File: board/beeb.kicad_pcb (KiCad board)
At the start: 2 copper layers, 76.2 x 53.3 mm, 54 parts, among them J2 AVR-JTAG-10, SW1 SW_DIP_x08, U1 WIT122UH, U2 ps2, U3 XC95144XL-TQ100, U4 beebKB, U5 LM1117-3.3, U6 74LS244_Split, U7 74LS244_Split, U8 LM2903

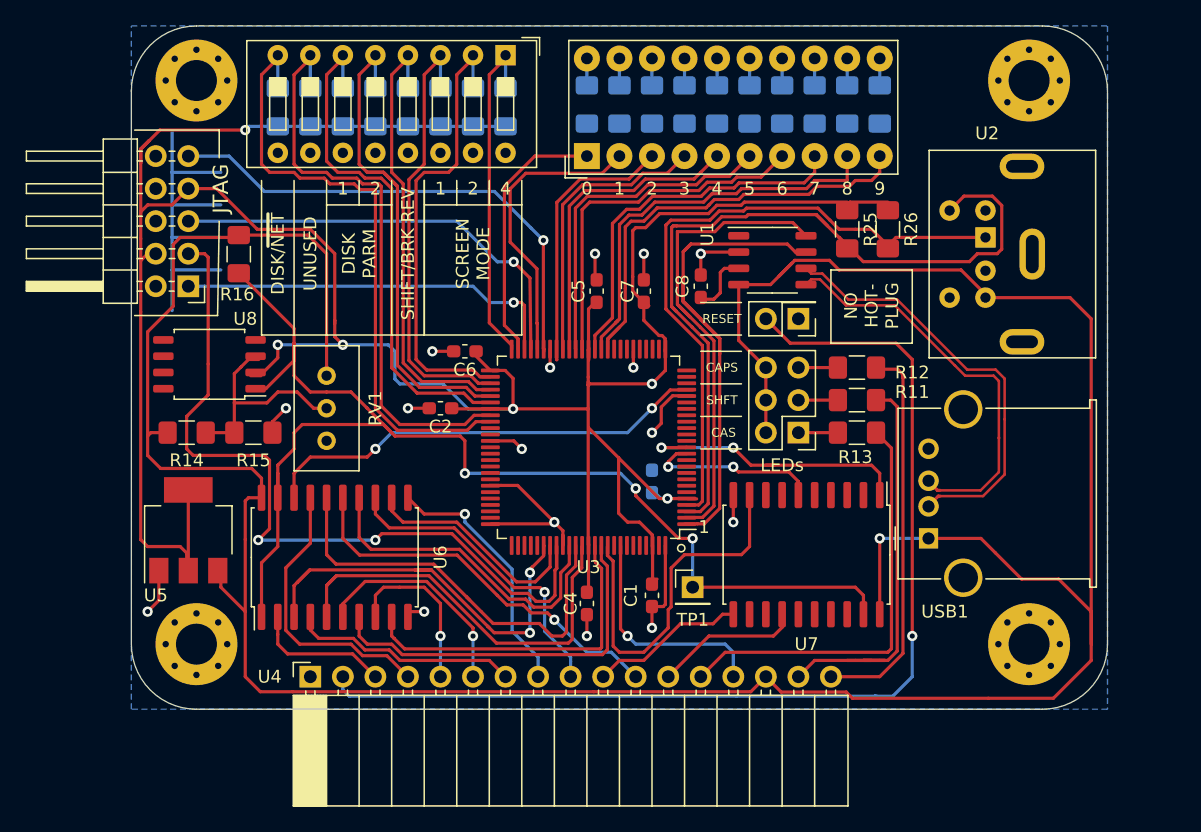
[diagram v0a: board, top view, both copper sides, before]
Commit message: Remove USB connector, move JTAG connector, mess about
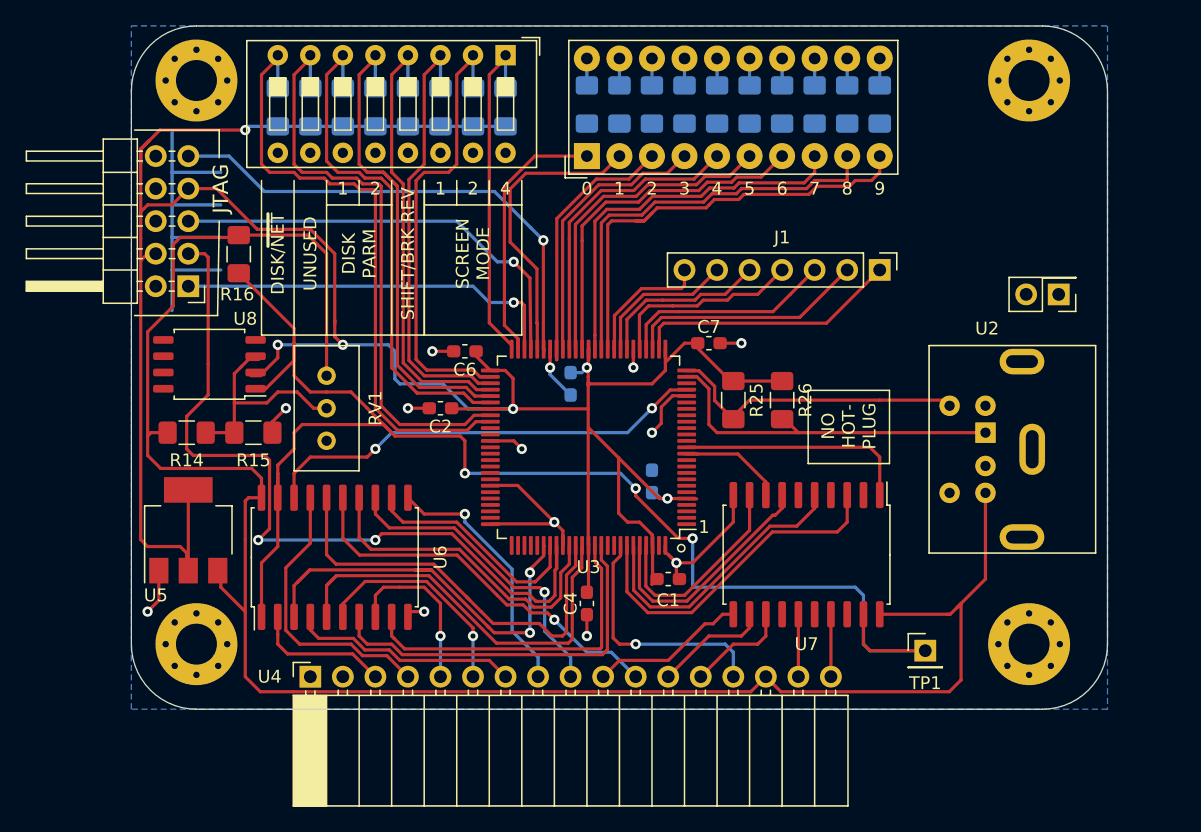
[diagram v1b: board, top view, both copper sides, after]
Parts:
- removed C8: 0.1uF, Capacitor_SMD:C_0603_1608Metric_Pad1.05x0.95mm_HandSolder
- removed LEDS1: J1, Connector_PinHeader_2.54mm:PinHeader_2x03_P2.54mm_Vertical
- removed R11, R12, R13: 470, Resistor_SMD:R_1206_3216Metric_Pad1.42x1.75mm_HandSolder
- removed U1: WIT122UH, Package_SO:SOP-8_3.9x4.9mm_P1.27mm
- removed USB1: USB, Connector_USB:USB_A_Molex_67643_Horizontal
- added J1: EXT, Connector_PinHeader_2.54mm:PinHeader_1x07_P2.54mm_Vertical, F.Cu at (105.4, 97.8)
- C5: moved to B.Cu
- moved RESET1 20.4 mm to (119.4, 99.7)
- moved TP1 18.8 mm to (109.0, 127.5)
- moved R25 16.0 mm to (94.0, 108.0)
- moved R26 15.7 mm to (97.8, 108.0)
- moved U2 15.2 mm to (113.7, 110.5)
- moved C5 7.52 mm to (81.3, 106.7), turned to 270 degrees
- moved C7 6.51 mm to (92.1, 103.5), turned to 0 degrees
- moved C1 1.80 mm to (88.9, 121.9), turned to 0 degrees
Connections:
- RESET1 pad 2: Net-(RESET1-Pad2) -> (no net)
- U3 pad 1: /PS2DATA_B -> (no net)
- U3 pad 2: /PS2CLK_B -> (no net)
- U3 pad 24: (no net) -> /PS2DATA_A
- U3 pad 25: (no net) -> /PS2CLK_A
- U3 pad 27: (no net) -> Net-(J1-Pad1)
- U3 pad 28: (no net) -> Net-(J1-Pad2)
- U3 pad 29: (no net) -> Net-(J1-Pad3)
- U3 pad 3: /PS2CLK_A -> (no net)
- U3 pad 30: (no net) -> Net-(J1-Pad4)
- U3 pad 32: (no net) -> Net-(J1-Pad5)
- U3 pad 33: (no net) -> Net-(J1-Pad6)
- U3 pad 34: (no net) -> Net-(J1-Pad7)
- U3 pad 4: /PS2DATA_A -> (no net)
- U3 pad 91: /ROW2_BUF -> (no net)
- U3 pad 94: (no net) -> /LED_CAPS_BUF
- U3 pad 95: (no net) -> /LED_SHIFT_BUF
- U3 pad 96: (no net) -> /LED_CAS_BUF
- U3 pad 97: (no net) -> /ROW2_BUF
- U4 pad 13: Net-(R13-Pad2) -> Net-(U4-Pad13)
- U4 pad 16: Net-(R11-Pad2) -> Net-(U4-Pad16)
- U4 pad 17: Net-(R12-Pad2) -> Net-(U4-Pad17)
- U4 pad 2: Net-(RESET1-Pad2) -> (no net)
- U7 pad 12: (no net) -> /W
- U7 pad 13: (no net) -> Net-(U4-Pad13)
- U7 pad 14: /W -> (no net)
- U7 pad 15: (no net) -> Net-(U4-Pad16)
- U7 pad 17: (no net) -> Net-(U4-Pad17)
- U7 pad 3: (no net) -> /LED_CAPS_BUF
- U7 pad 5: (no net) -> /LED_SHIFT_BUF
- U7 pad 6: /W_BUF -> (no net)
- U7 pad 7: (no net) -> /LED_CAS_BUF
- U7 pad 8: (no net) -> /W_BUF
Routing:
- net +5V: track 241.3 -> 153.4 mm, vias 1 -> 0
- net Net-(RESET1-Pad2): track 83.9 -> 0.00 mm, vias 1 -> 0
- net /PS2DATA_B: track 43.5 -> 0.00 mm
- net /PS2CLK_A: track 63.9 -> 24.2 mm
- net /PS2CLK_B: track 37.3 -> 0.00 mm
- net Net-(R11-Pad2): track 34.8 -> 0.00 mm
- net /USB_N: track 33.7 -> 0.00 mm
- net Net-(R13-Pad2): track 33.2 -> 0.00 mm
- net /USB_P: track 32.0 -> 0.00 mm
- net Net-(R12-Pad2): track 30.3 -> 0.00 mm
- net /LED_CAPS_BUF: track 0.00 -> 26.3 mm
- net +3V3: track 233.7 -> 210.0 mm
- net /PS2DATA_A: track 51.1 -> 28.7 mm
- net /LED_SHIFT_BUF: track 0.00 -> 22.3 mm
- net Net-(J1-Pad1): track 0.00 -> 20.9 mm
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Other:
- board text removed: "CAPS"
- board text removed: "CAS"
- board text removed: "LEDs"
- board text removed: "RESET"
- board text removed: "SHFT"

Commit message: Add reset line, remov vref pot
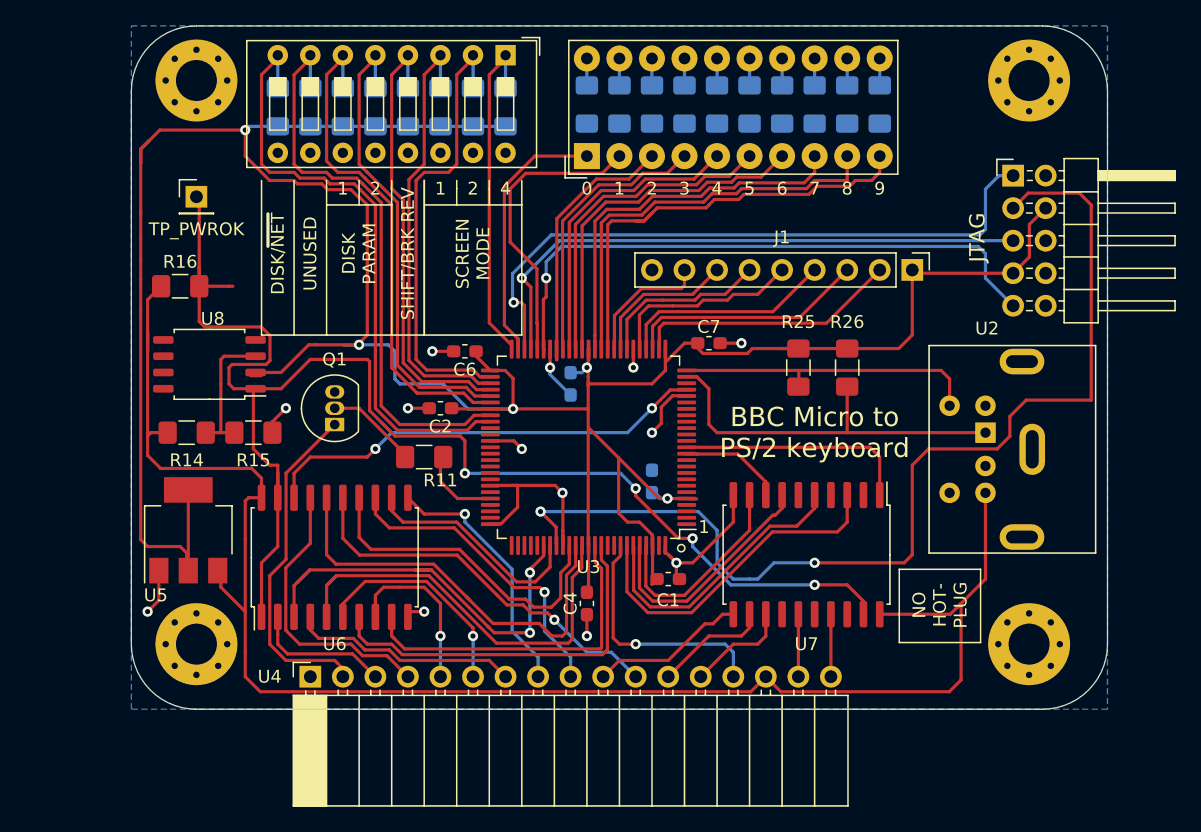
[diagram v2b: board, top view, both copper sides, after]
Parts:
- removed RESET1: J3, Connector_PinHeader_2.54mm:PinHeader_2x01_P2.54mm_Vertical
- removed RV1: R_POT, Potentiometer_THT:Potentiometer_Bourns_3386C_Horizontal
- added Q1: BC337, Package_TO_SOT_THT:TO-92_Inline, F.Cu at (62.9, 109.9)
- added R11: 220, Resistor_SMD:R_1206_3216Metric_Pad1.42x1.75mm_HandSolder, F.Cu at (69.8, 112.4)
- J1: value EXT -> Conn_01x09_Male; footprint Connector_PinHeader_2.54mm:PinHeader_1x07_P2.54mm_Vertical -> Connector_PinHeader_2.54mm:PinHeader_1x09_P2.54mm_Vertical
- moved TP1 67.0 mm to (52.1, 92.1)
- moved J2 65.0 mm to (115.8, 90.4), turned to 0 degrees
- moved R25 5.68 mm to (99.1, 105.4)
- moved R26 5.68 mm to (102.9, 105.4)
- moved R16 5.21 mm to (50.8, 99.1), turned to 0 degrees
- moved J1 2.54 mm to (108.0, 97.8)
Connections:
- J1 pad 1: Net-(J1-Pad1) -> +3V3
- U3 pad 27: Net-(J1-Pad1) -> Net-(J1-Pad2)
- U3 pad 28: Net-(J1-Pad2) -> Net-(J1-Pad3)
- U3 pad 29: Net-(J1-Pad3) -> Net-(J1-Pad4)
- U3 pad 30: Net-(J1-Pad4) -> Net-(J1-Pad5)
- U3 pad 32: Net-(J1-Pad5) -> Net-(J1-Pad6)
- U3 pad 33: Net-(J1-Pad6) -> Net-(J1-Pad7)
- U3 pad 34: Net-(J1-Pad7) -> Net-(J1-Pad8)
- U3 pad 71: (no net) -> /RST
- U4 pad 2: (no net) -> Net-(Q1-Pad1)
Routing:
- net +3V3: track 210.0 -> 238.5 mm, vias 6 -> 5
- net GND: track 84.4 -> 56.7 mm
- net Net-(Q1-Pad1): track 0.00 -> 26.4 mm
- net +5V: track 153.4 -> 128.1 mm
- net Net-(J1-Pad1): track 20.9 -> 0.00 mm
- net /TDO: track 62.2 -> 82.9 mm
- net /TCK: track 30.3 -> 50.7 mm
- net /TMS: track 34.7 -> 45.4 mm
- net Net-(J1-Pad8): track 0.00 -> 10.3 mm
- net /TDI: track 39.1 -> 47.1 mm
- net Net-(Q1-Pad2): track 0.00 -> 7.20 mm
- net Net-(R14-Pad2): track 17.4 -> 10.9 mm
- net /RST: track 0.00 -> 6.35 mm
- net Net-(R20-Pad2): track 41.6 -> 36.8 mm
- net Net-(J1-Pad2): track 18.8 -> 20.9 mm
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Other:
- board text added: "BBC Micro to PS/2 keyboard"
- board text added: "DISK PARAM"
- board text removed: "BBC Micro to PS/2 and USB keyboard"
- board text removed: "DISK PARM"

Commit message: Connect U8 to power/gnd, change U6 and U7 footprint, add TP_CLKBUF, tidy
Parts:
- added TP2: TP_CLKBUF, Connector_PinHeader_2.54mm:PinHeader_1x01_P2.54mm_Vertical, F.Cu at (95.2, 108.0)
- Q1: footprint Package_TO_SOT_THT:TO-92_Inline -> Package_TO_SOT_THT:TO-92_Inline_Wide
- U6, U7: footprint Package_SO:SOIC-20W_7.5x12.8mm_P1.27mm -> beeb:beeb_SO-20_5.3x12.6mm_P1.27mm
- U8: footprint Package_SO:SOP-8_5.28x5.23mm_P1.27mm -> Package_SO:SOP-8_3.76x4.96mm_P1.27mm
- moved Q1 1.27 mm to (62.9, 111.1)
- moved R16 0.64 mm to (50.8, 98.4)
- moved U8 0.46 mm to (53.3, 104.8), turned to 270 degrees
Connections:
- U8 pad 4: (no net) -> GND
- U8 pad 8: (no net) -> +5V
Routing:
- net /PWROK: track 112.8 -> 101.7 mm
- net +5V: track 128.1 -> 137.6 mm
- net /TCK: track 50.7 -> 57.0 mm
- net /BEEBCLK_BUF: track 36.4 -> 42.6 mm
- net /TMS: track 45.4 -> 51.0 mm
- net /LED2: track 23.0 -> 18.1 mm
- net /TDO: track 82.9 -> 78.6 mm
- net Net-(R14-Pad2): track 10.9 -> 15.1 mm
- net /COL0: track 14.1 -> 10.8 mm
- net /CB_BUF: track 34.1 -> 32.3 mm
- net /W_BUF: track 8.28 -> 9.75 mm
- net /COL2_BUF: track 33.3 -> 32.0 mm
- net GND: track 56.7 -> 55.4 mm, vias 13 -> 14
- net /ROW3: track 30.5 -> 29.2 mm
- net /CB: track 22.2 -> 20.9 mm
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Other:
- board text added: "27"
- board text added: "28"
- board text added: "29"
- board text added: "3.3v"
- board text added: "30"
- board text added: "32"
- board text added: "33"
- board text added: "34"
- board text added: "BBC Micro to PS/2 keyboard Aliz Hammond"
- board text added: "GND"
- board text removed: "BBC Micro to PS/2 keyboard"

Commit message: Tidy schematic a little
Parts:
- R17, R18, R19, R20, R21, R22, R23, R24: value R_Small -> 10K
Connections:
- SW1 pad 1: Net-(R24-Pad2) -> Net-(R17-Pad2)
- SW1 pad 2: Net-(R23-Pad2) -> Net-(R18-Pad2)
- SW1 pad 3: Net-(R22-Pad2) -> Net-(R19-Pad2)
- SW1 pad 4: Net-(R21-Pad2) -> Net-(R20-Pad2)
- SW1 pad 5: Net-(R20-Pad2) -> Net-(R21-Pad2)
- SW1 pad 6: Net-(R19-Pad2) -> Net-(R22-Pad2)
- SW1 pad 7: Net-(R18-Pad2) -> Net-(R23-Pad2)
- SW1 pad 8: Net-(R17-Pad2) -> Net-(R24-Pad2)
- U3 pad 50: Net-(R24-Pad2) -> Net-(R17-Pad2)
- U3 pad 52: Net-(R23-Pad2) -> Net-(R18-Pad2)
- U3 pad 53: Net-(R22-Pad2) -> Net-(R19-Pad2)
- U3 pad 54: Net-(R21-Pad2) -> Net-(R20-Pad2)
- U3 pad 55: Net-(R20-Pad2) -> Net-(R21-Pad2)
- U3 pad 56: Net-(R19-Pad2) -> Net-(R22-Pad2)
- U3 pad 58: Net-(R18-Pad2) -> Net-(R23-Pad2)
- U3 pad 59: Net-(R17-Pad2) -> Net-(R24-Pad2)

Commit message: correct inverted dip sw
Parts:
- R1, R10, R2, R3, R4, R5, R6, R7, R8, R9: value R -> 10K
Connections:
- SW1 pad 1: Net-(R17-Pad2) -> Net-(R24-Pad2)
- SW1 pad 2: Net-(R18-Pad2) -> Net-(R23-Pad2)
- SW1 pad 3: Net-(R19-Pad2) -> Net-(R22-Pad2)
- SW1 pad 4: Net-(R20-Pad2) -> Net-(R21-Pad2)
- SW1 pad 5: Net-(R21-Pad2) -> Net-(R20-Pad2)
- SW1 pad 6: Net-(R22-Pad2) -> Net-(R19-Pad2)
- SW1 pad 7: Net-(R23-Pad2) -> Net-(R18-Pad2)
- SW1 pad 8: Net-(R24-Pad2) -> Net-(R17-Pad2)
- U3 pad 50: Net-(R17-Pad2) -> Net-(R24-Pad2)
- U3 pad 52: Net-(R18-Pad2) -> Net-(R23-Pad2)
- U3 pad 53: Net-(R19-Pad2) -> Net-(R22-Pad2)
- U3 pad 54: Net-(R20-Pad2) -> Net-(R21-Pad2)
- U3 pad 55: Net-(R21-Pad2) -> Net-(R20-Pad2)
- U3 pad 56: Net-(R22-Pad2) -> Net-(R19-Pad2)
- U3 pad 58: Net-(R23-Pad2) -> Net-(R18-Pad2)
- U3 pad 59: Net-(R24-Pad2) -> Net-(R17-Pad2)
